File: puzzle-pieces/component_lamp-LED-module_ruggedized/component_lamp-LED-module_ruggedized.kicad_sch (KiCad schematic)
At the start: 15 parts, among them J4 Conn_01x02_Pin, J5 Conn_01x02_Pin

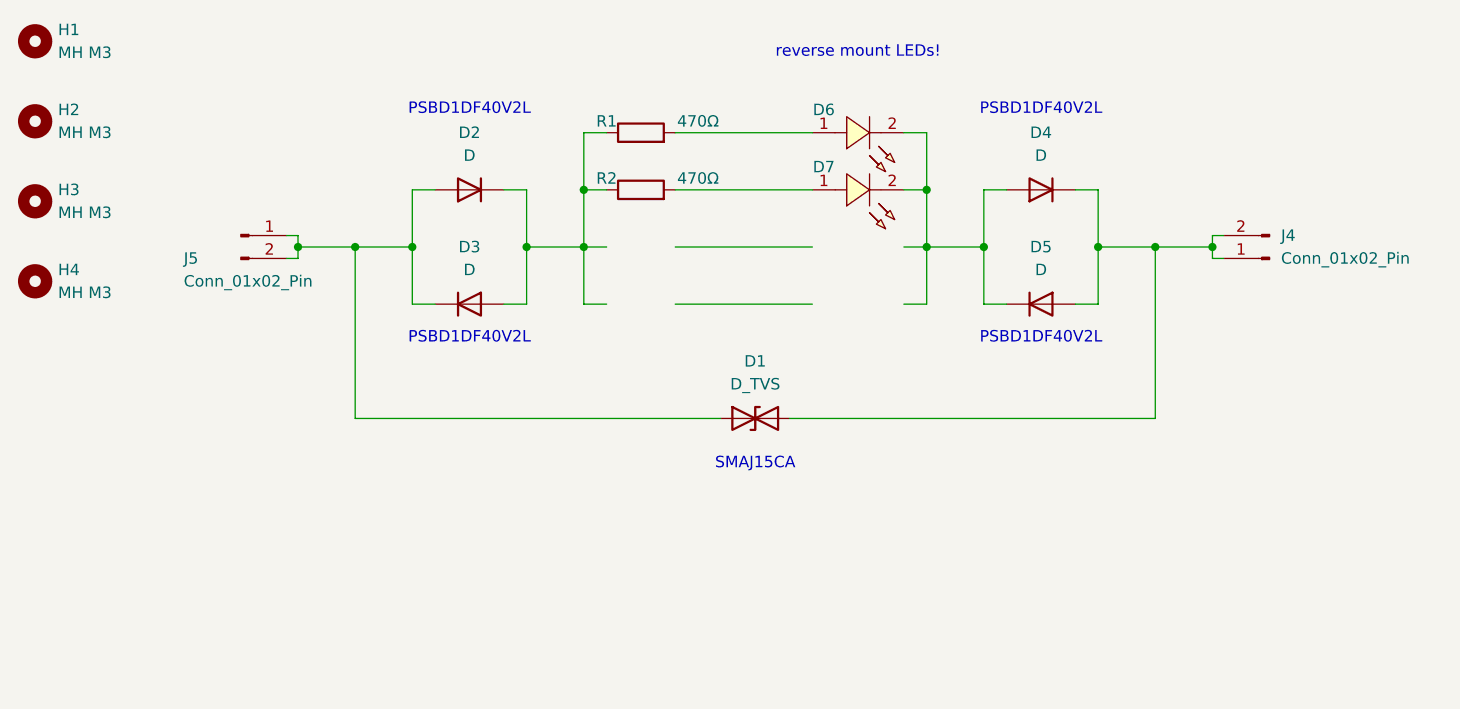
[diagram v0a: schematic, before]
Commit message: Update LED-module PCB and schematic layout
Apply extensive layout and schematic updates for the ruggedized LED module: reposition footprints/text/pads, correct nets and pinfunction names, add unit declarations, remove placeholder Datasheet ~, adjust zone/polygon shapes and priorities, and remove some Edge.Cuts circles. Update schematic generator/version and many symbol properties (show_name, do_not_autoplace, in_pos_files, hide). Update .kicad_pro sheet UUID/name and add 0.75mm track width option. Numerous coordinate, uuid and silk/FP_line corrections to sync PCB and schematic placement.
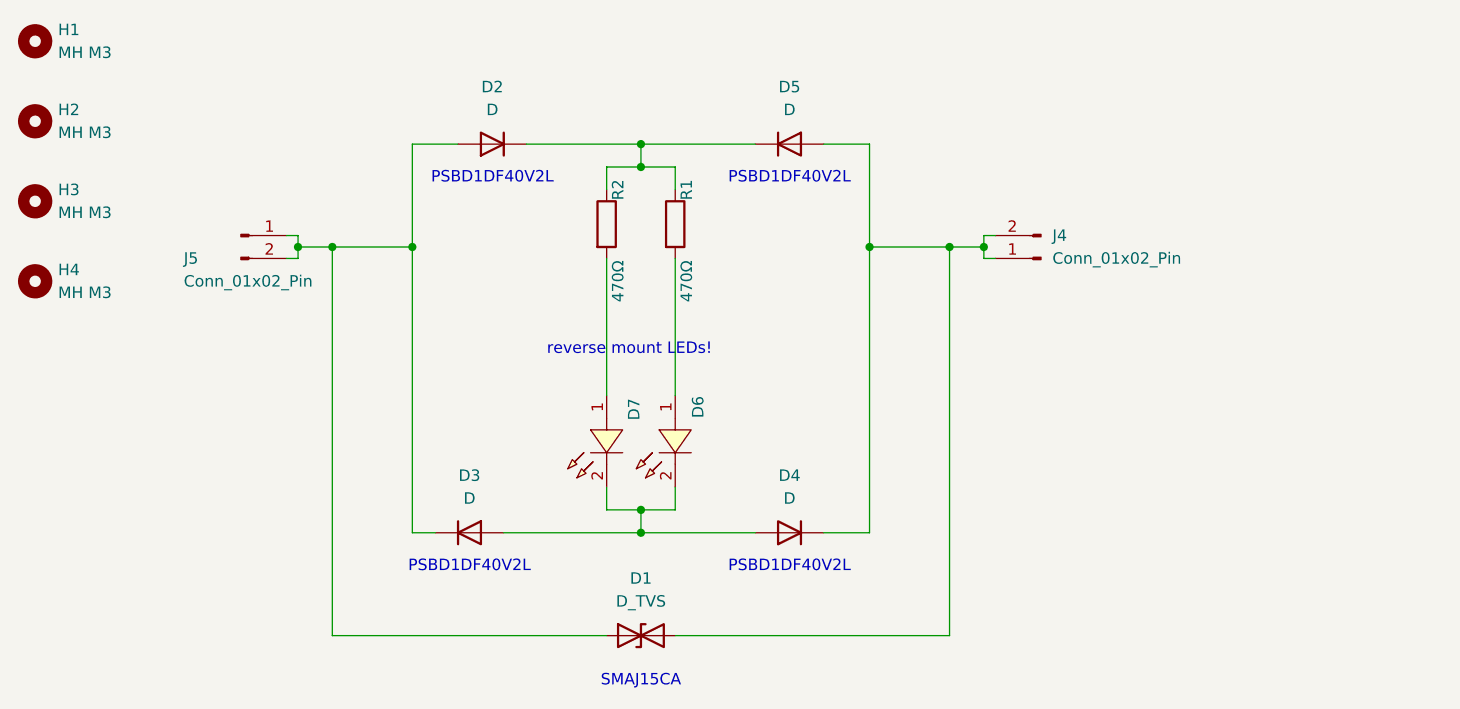
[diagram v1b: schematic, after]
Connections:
- net at D4.2 (A), D6.2, D7.2: now also D3.2 (A); no longer D5.1 (K)
- net at D2.1 (K), R1.1, R2.1: now also D5.1 (K); no longer D3.2 (A)
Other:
- moved on the sheet: D1, D2, D3, D4, D5, D6, D7, J4, R1, R2
